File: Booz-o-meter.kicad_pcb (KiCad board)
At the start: 2 copper layers, 101.6 x 76.2 mm, 61 parts, among them J1 Power, J4 Rod, K1 G5V-2, K2 G5V-2, K3 G5V-2, K4 G5V-2, K5 G5V-2, K6 G5V-2, K7 G5V-2, K8 G5V-2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

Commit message: First pass at routing
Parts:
- added H1: MountingHole, MountingHole:MountingHole_3.5mm, F.Cu at (55.9, 45.7)
- added H2: MountingHole, MountingHole:MountingHole_3.5mm, F.Cu at (147.3, 45.7)
- added H3: MountingHole, MountingHole:MountingHole_3.5mm, F.Cu at (147.3, 132.1)
- added H4: MountingHole, MountingHole:MountingHole_3.5mm, F.Cu at (55.9, 132.1)
- K1: value G5V-2 -> GAME_ACTIVE1
- K2: value G5V-2 -> GAME_OVER
- K3: value G5V-2 -> ZAPOSC
- K4: value G5V-2 -> GAME_ACTIVE2
- K5: value G5V-2 -> FWD
- K6: value G5V-2 -> LOST
- K7: value G5V-2 -> REV
- K8: value G5V-2 -> WON
- K9: value G5V-2 -> GAME_RESET
- moved D15 34.2 mm to (66.0, 102.9), turned to -90 degrees
- moved D10 10.5 mm to (100.3, 111.8)
- moved D23 9.25 mm to (99.1, 58.4)
- moved D22 8.89 mm to (133.3, 54.6)
- moved R9 5.08 mm to (109.2, 99.1), turned to 180 degrees
- moved C2 5.00 mm to (99.0, 104.1), turned to 180 degrees
- moved D9 2.54 mm to (109.2, 121.9)
- moved Q1 2.54 mm to (86.4, 106.7)
- moved R13 2.54 mm to (88.9, 111.8)
- moved R14 2.54 mm to (81.3, 111.8)
- moved R4 2.54 mm to (111.8, 116.8)
- moved D21 2.54 mm to (90.2, 55.9), turned to -90 degrees
- moved GAME_OVER_TIMER1 2.54 mm to (73.7, 106.7)
- renumbered RV1 to GAME_OVER_TIMER1
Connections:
- D24 pad 1: unconnected-(D24-K-Pad1) -> Net-(D24-K)
- K1 pad 1: /game_active -> VCC
- K1 pad 16: VCC -> /game_active
- K1 pad 9: Net-(K1-Pad9) -> Net-(D24-K)
- K7 pad 1: Net-(K1-Pad9) -> Net-(D24-K)
- PB_RESET1 pad 3: unconnected-(PB_RESET1-K-Pad3) -> Net-(D9-KA)
- PB_RESET1 pad 4: unconnected-(PB_RESET1-A-Pad4) -> Net-(D9-AK)
- R10 pad 1: Net-(K1-Pad9) -> Net-(D24-K)
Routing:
- net GND: track 0.00 -> 243.2 mm, vias 0 -> 1
- net /game_lost: track 0.00 -> 186.7 mm
- net Net-(BZ1-+): track 0.00 -> 171.3 mm, vias 0 -> 2
- net /game_active: track 0.00 -> 171.2 mm, vias 0 -> 1
- net ROD_START: track 0.00 -> 150.0 mm, vias 0 -> 2
- net Net-(D9-AK): track 0.00 -> 144.7 mm, vias 0 -> 1
- net Net-(J4-Pin_3): track 0.00 -> 138.4 mm, vias 0 -> 1
- net /game_won: track 0.00 -> 106.0 mm, vias 0 -> 2
- net Net-(D19-K): track 0.00 -> 99.2 mm, vias 0 -> 1
- net Net-(D9-KA): track 0.00 -> 90.6 mm, vias 0 -> 1
- net Net-(D24-K): track 0.00 -> 87.4 mm, vias 0 -> 1
- net ROD_MIDDLE: track 0.00 -> 83.0 mm, vias 0 -> 3
- net Net-(SW_ZAP_ON_TOUCH1-B): track 0.00 -> 80.6 mm, vias 0 -> 2
- net Net-(D13-K): track 0.00 -> 78.3 mm, vias 0 -> 1
- net V_trans: track 0.00 -> 75.3 mm, vias 0 -> 1
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- added copper zone on B.Cu, net VCC
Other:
- board size 101.6 x 76.2 mm -> 101.6 x 96.5 mm
- rule pad_to_mask_clearance: 0 -> 0.0508
- board text added: "12V"
- board text added: "GND"
- board text added: "VMOTOR"
- board text added: "VTRANS"

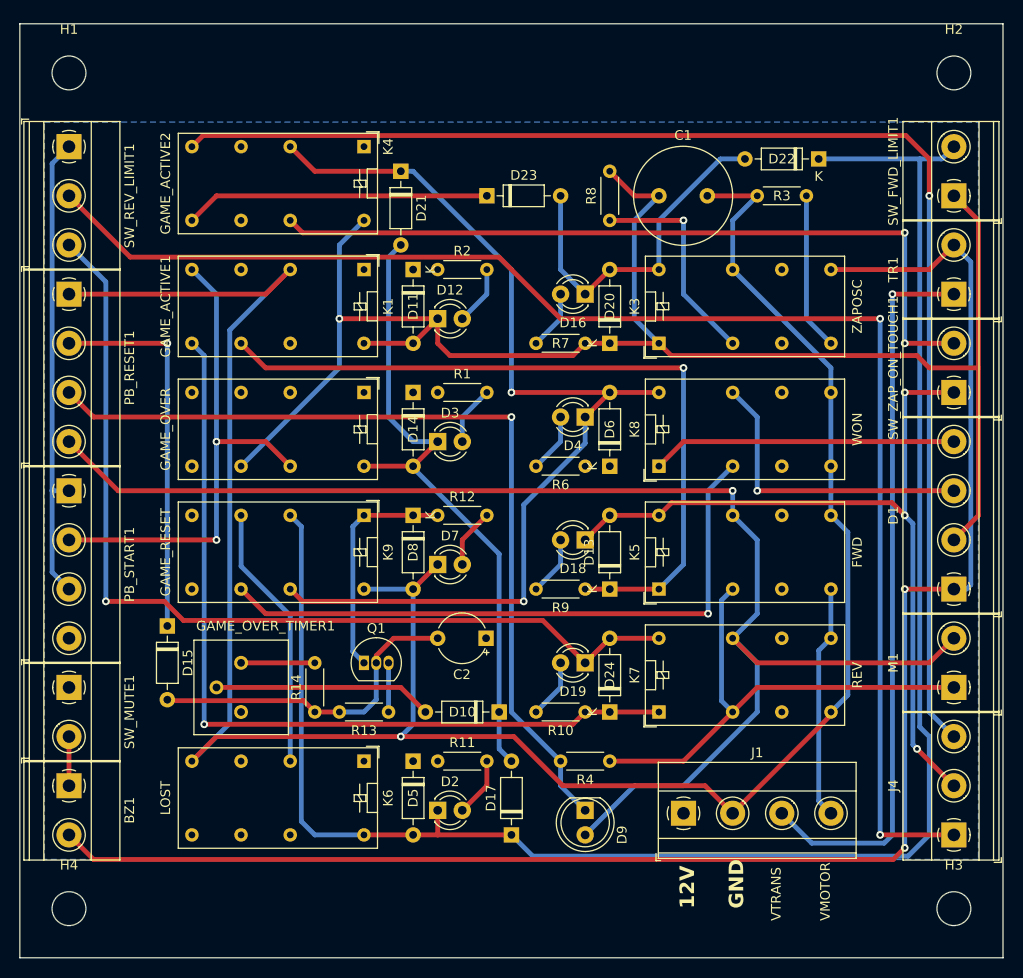
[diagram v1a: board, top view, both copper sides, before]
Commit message: Fix zap on touch, add motor series R, clean DRC
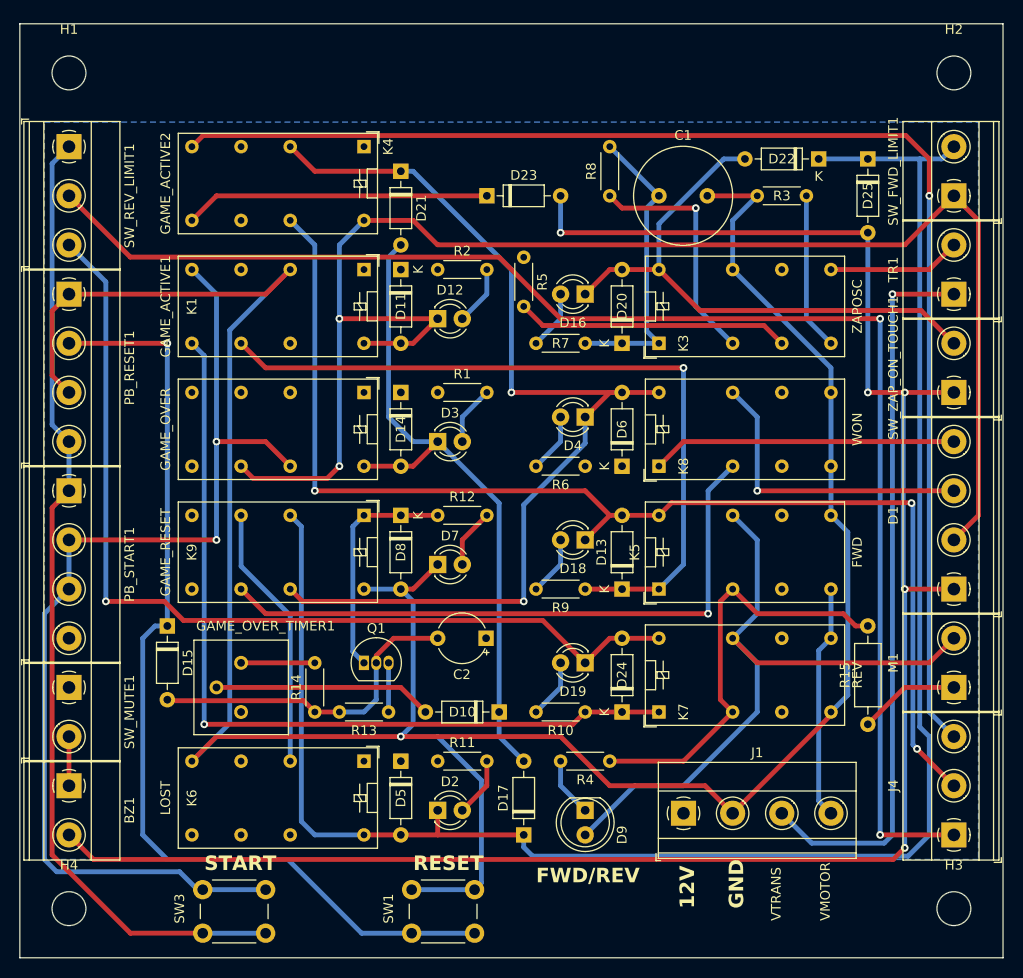
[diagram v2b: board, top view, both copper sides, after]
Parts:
- added D25: 1N914, Diode_THT:D_DO-35_SOD27_P7.62mm_Horizontal, F.Cu at (138.4, 54.6)
- added R15: 1k, Resistor_THT:R_Axial_DIN0207_L6.3mm_D2.5mm_P10.16mm_Horizontal, F.Cu at (138.4, 113.0)
- added R5: 10, Resistor_THT:R_Axial_DIN0204_L3.6mm_D1.6mm_P5.08mm_Horizontal, F.Cu at (102.9, 64.8)
- added SW1: SW_TEST_RESET, Button_Switch_THT:SW_PUSH_6mm, F.Cu at (97.8, 134.6)
- added SW3: SW_TEST_START, Button_Switch_THT:SW_PUSH_6mm, F.Cu at (69.7, 130.1)
- R8: value 100k -> 10
- moved R8 2.54 mm to (111.8, 58.4)
- moved D17 1.27 mm to (102.9, 124.5)
- moved D11 1.27 mm to (90.2, 66.0)
- moved D13 1.27 mm to (113.0, 99.1)
- moved D14 1.27 mm to (90.2, 78.7)
- moved D20 1.27 mm to (113.0, 73.7)
- moved D24 1.27 mm to (113.0, 111.8)
- moved D5 1.27 mm to (90.2, 116.8)
- moved D6 1.27 mm to (113.0, 86.4)
- moved D8 1.27 mm to (90.2, 91.4)
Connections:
- C1 pad 1: /game_active -> Net-(D20-K)
- D20 pad 1: /game_active -> Net-(D20-K)
- D23 pad 2: Net-(D16-K) -> Net-(BZ1-+)
- K1 pad 8: Net-(SW1-A) -> Net-(PB_START1-K)
- K2 pad 13: Net-(SW1-A) -> Net-(PB_START1-K)
- K3 pad 1: /game_active -> Net-(D20-K)
- K3 pad 6: VCC -> Net-(K3-Pad6)
- K3 pad 9: Net-(BZ1-+) -> Net-(K3-Pad9)
- K4 pad 13: Net-(SW_ZAP_ON_TOUCH1-B) -> ROD_MIDDLE
- K5 pad 4: Net-(M1-+) -> Net-(K5-Pad4)
- K7 pad 4: Net-(M1-+) -> Net-(K5-Pad4)
- PB_RESET1 pad 3: Net-(D9-KA) -> GND
- PB_RESET1 pad 4: Net-(D9-AK) -> Net-(PB_RESET1-A)
- PB_START1 pad 1: Net-(PB_START1-K) -> Net-(PB_RESET1-A)
- PB_START1 pad 2: Net-(SW1-A) -> Net-(PB_START1-K)
- R4 pad 1: Net-(M1-+) -> Net-(K5-Pad4)
- R7 pad 1: /game_active -> Net-(D20-K)
- R8 pad 2: /game_active -> Net-(D20-K)
- SW_REV_LIMIT1 pad 1: Net-(PB_START1-K) -> Net-(PB_RESET1-A)
- SW_ZAP_ON_TOUCH1 pad 1: ROD_MIDDLE -> Net-(BZ1-+)
- SW_ZAP_ON_TOUCH1 pad 2: Net-(SW_ZAP_ON_TOUCH1-B) -> Net-(D16-K)
- TR1 pad 2: Net-(BZ1-+) -> Net-(K3-Pad9)
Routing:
- net Net-(PB_RESET1-A): track 0.00 -> 100.8 mm
- net Net-(D9-KA): track 90.6 -> 6.13 mm, vias 1 -> 0
- net Net-(SW_ZAP_ON_TOUCH1-B): track 80.6 -> 0.00 mm, vias 2 -> 0
- net Net-(D9-AK): track 144.7 -> 71.5 mm, vias 1 -> 0
- net Net-(PB_START1-K): track 48.9 -> 111.1 mm, vias 0 -> 2
- net Net-(D15-K): track 39.4 -> 101.3 mm
- net Net-(SW1-A): track 52.9 -> 0.00 mm, vias 2 -> 0
- net Net-(K5-Pad4): track 0.00 -> 44.1 mm
- net ROD_MIDDLE: track 83.0 -> 126.9 mm
- net Net-(M1-+): track 52.4 -> 10.5 mm
- net GND: track 243.2 -> 283.6 mm
- net Net-(D20-K): track 0.00 -> 31.1 mm
- net Net-(BZ1-+): track 171.3 -> 201.1 mm, vias 2 -> 5
- net Net-(K3-Pad6): track 0.00 -> 28.2 mm
- net Net-(D16-K): track 36.5 -> 58.7 mm
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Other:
- board text added: "FWD/REV"
- board text added: "RESET"
- board text added: "START"

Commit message: Increase resistor pitch to 0.4, add silk text
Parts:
- R1, R10, R11, R12, R13, R14, R2, R3, R4, R5, R6, R7, R8, R9: footprint Resistor_THT:R_Axial_DIN0204_L3.6mm_D1.6mm_P5.08mm_Horizontal -> Resistor_THT:R_Axial_DIN0207_L6.3mm_D2.5mm_P10.16mm_Horizontal
- moved D17 69.2 mm to (94.0, 55.9), turned to -90 degrees
- moved R1 10.2 mm to (99.1, 87.6), turned to 90 degrees
- moved R2 10.2 mm to (99.1, 74.9), turned to 90 degrees
- moved R13 9.67 mm to (85.1, 102.9), turned to 0 degrees
- moved D22 7.73 mm to (134.6, 62.2)
- moved D10 7.62 mm to (92.7, 111.8)
- moved R7 5.24 mm to (104.1, 74.9), turned to 90 degrees
- moved R12 5.24 mm to (99.1, 90.2), turned to -90 degrees
- moved R6 5.24 mm to (104.1, 87.6), turned to 90 degrees
- moved R9 5.24 mm to (104.1, 100.3), turned to 90 degrees
- moved C2 4.60 mm to (101.6, 108.0)
- moved D23 4.02 mm to (97.8, 54.6), turned to -90 degrees
- moved R10 4.02 mm to (105.4, 113.0), turned to 90 degrees
- moved R5 4.02 mm to (101.6, 61.0), turned to 0 degrees
- moved D18 3.81 mm to (109.2, 90.2), turned to -90 degrees
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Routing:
- net VCC: track 36.6 -> 85.0 mm
- net /game_lost: track 187.4 -> 155.0 mm, vias 0 -> 1
- net Net-(D20-K): track 31.1 -> 46.3 mm
- net /game_active: track 158.3 -> 144.5 mm
- net Net-(D8-K): track 23.8 -> 32.6 mm
- net Net-(D15-A): track 34.1 -> 42.3 mm
- net Net-(D16-K): track 58.7 -> 50.7 mm, vias 0 -> 1
- net Net-(BZ1-+): track 201.1 -> 208.3 mm, vias 5 -> 4
- net Net-(D10-A): track 22.6 -> 15.8 mm
- net Net-(K8-Pad4): track 65.6 -> 59.0 mm
- net /game_over: track 69.8 -> 76.0 mm, vias 0 -> 1
- net Net-(K3-Pad4): track 25.0 -> 31.0 mm
- net Net-(D19-K): track 99.2 -> 105.0 mm
- net Net-(D13-K): track 78.3 -> 83.9 mm
- net Net-(K3-Pad6): track 28.2 -> 23.0 mm, vias 0 -> 1
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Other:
- board text added: "+"
- board text added: "B"
- board text added: "BUZZER"
- board text added: "C"
- board text added: "G"
- board text added: "LED+"
- board text added: "LED-"
- board text added: "MOTOR"
- board text added: "MUTE"
- board text added: "NC"
- board text added: "NO"
- board text added: "PB_START"
- board text added: "R"
- board text added: "REV"
- board text added: "ROD MID"
- board text added: "ROD START"
- board text added: "ROD WIN"
- board text added: "SW ZAP TOUCH"

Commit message: Final tweaks before send out
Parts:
- added D26: 1N914, Diode_THT:D_DO-35_SOD27_P7.62mm_Horizontal, F.Cu at (99.7, 121.3)
- D1: value LED_RBGA -> LED_RGBA
- K1: value GAME_ACTIVE1 -> G5V-2
- K2: value GAME_OVER -> G5V-2
- K3: value ZAPOSC -> G5V-2
- K4: value GAME_ACTIVE2 -> G5V-2
- K5: value FWD -> G5V-2
- K6: value LOST -> G5V-2
- K7: value REV -> G5V-2
- K8: value WON -> G5V-2
- K9: value GAME_RESET -> G5V-2
- R15: value 1k -> 5
- moved SW1 2.54 mm to (95.2, 134.6)
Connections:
- net Net-(J4-Pin_3) renamed ROD_WIN
- D1 pad 2: /game_active -> Net-(D1-GK)
- D1 pad 3: Net-(D1-GK) -> /game_active
- K1 pad 11: Net-(D13-K) -> Net-(D24-K)
- K1 pad 9: Net-(D24-K) -> Net-(D13-K)
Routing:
- net /game_over: track 76.0 -> 87.5 mm
- net Net-(D24-K): track 87.0 -> 97.1 mm, vias 2 -> 1
- net Net-(D13-K): track 83.9 -> 75.4 mm
- net /game_active: track 144.5 -> 139.5 mm
- net Net-(D15-K): track 101.3 -> 106.3 mm
- net Net-(D1-GK): track 31.5 -> 35.5 mm
- net Net-(D2-A): track 9.72 -> 11.2 mm
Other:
- board text added: "Booz-O-Meter"
- board text added: "FWD"
- board text added: "GAME ACTIVE 1"
- board text added: "GAME ACTIVE 2"
- board text added: "GAME OVER"
- board text added: "GAME OVER TMR"
- board text added: "GAME RESET"
- board text added: "V1.0 2/13/2024 www.spuriousemissions.com @spurious_emissions"
- board text added: "WON"
- board text added: "ZAP OSC"
